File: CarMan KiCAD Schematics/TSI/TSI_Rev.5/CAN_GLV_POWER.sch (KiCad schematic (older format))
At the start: 50 parts, among them J31 Cooling Jumper, K2 G5LE-1-E, K3 SFS2-DC24V, K4 SFS2-DC24V, Q11 TN2130K1-G, U14 Bottom Left, U15 Top Left, U17 Top Right, U2 Bottom Right, U20 TLP293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

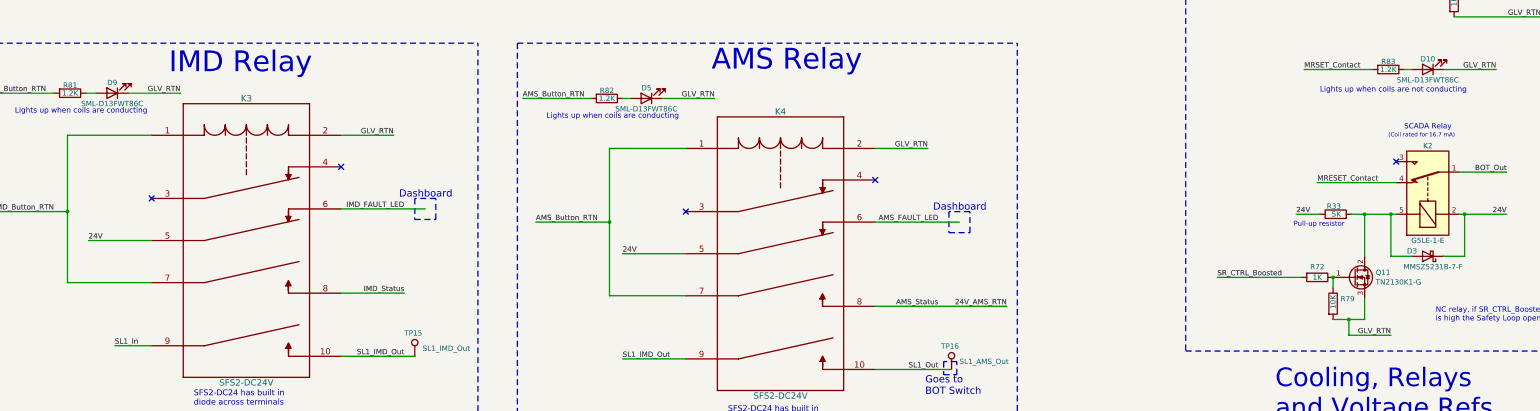
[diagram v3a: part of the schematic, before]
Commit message: - Removed pull up resistor  - Changed the relay leds such that they are the ones logic and GLV Bob use
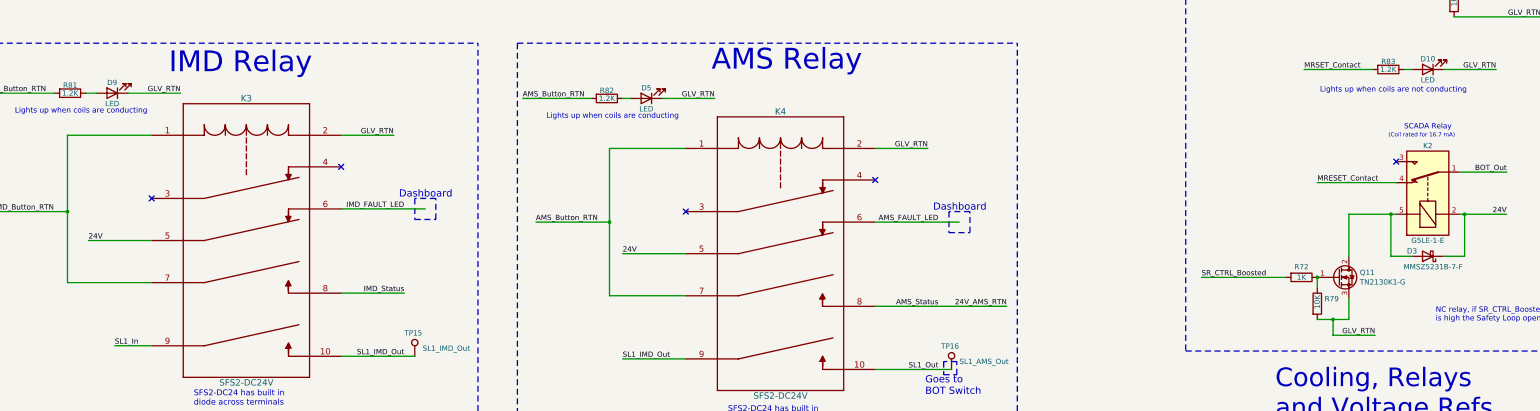
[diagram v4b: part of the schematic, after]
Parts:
- removed R33: 5K, Resistor_SMD:R_0805_2012Metric_Pad1.15x1.40mm_HandSolder, symbol Device:R
- D10, D5, D9: value SML-D13FWT86C -> LED; footprint LED_SMD:LED_0603_1608Metric -> LED_SMD:LED_0805_2012Metric_Pad1.15x1.40mm_HandSolder; Part Name (none) -> VAOL-S8GT4
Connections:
- wire segments 200 -> 198
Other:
- note removed: "Pull-up resistor"
- moved on the sheet: Q11, R72, R79
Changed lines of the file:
@@
 L Device:Q_NMOS_GDS Q11
 U 1 1 5FB4C495
-P 13650 9150
-F 0 "Q11" H 13854 9196 50  0000 L CNN
-F 1 "TN2130K1-G" H 13854 9105 50  0000 L CNN
-F 2 "TSI_Rev_2021_Footprint_Lib:SOT95P237X112-3N" H 13850 9250 50  0001 C CNN
-F 3 "https://ww1.microchip.com/downloads/en/DeviceDoc/TN2130-N-Channel-Enhancement-Mode-Vertical-DMOS-FET-Data-Sheet-20005944B.pdf" H 13650 9150 50  0001 C CNN
-	1    13650 9150
-	1    0    0    -1
-$EndComp
-Text Label 12350 9150 0    50   ~ 0
+P 13500 9150
+F 0 "Q11" H 13704 9196 50  0000 L CNN
+F 1 "TN2130K1-G" H 13704 9105 50  0000 L CNN
+F 2 "TSI_Rev_2021_Footprint_Lib:SOT95P237X112-3N" H 13700 9250 50  0001 C CNN
+F 3 "https://ww1.microchip.com/downloads/en/DeviceDoc/TN2130-N-Channel-Enhancement-Mode-Vertical-DMOS-FET-Data-Sheet-20005944B.pdf" H 13500 9150 50  0001 C CNN
+	1    13500 9150
+	1    0    0    -1
+$EndComp
+Text Label 12200 9150 0    50   ~ 0
 SR_CTRL_Boosted
 $Comp
@@
 L Device:R R72
 U 1 1 5FB6696B
-P 13300 9150
-F 0 "R72" V 13200 9150 50  0000 C CNN
-F 1 "1K" V 13300 9150 50  0000 C CNN
-F 2 "Resistor_SMD:R_0805_2012Metric_Pad1.15x1.40mm_HandSolder" V 13230 9150 50  0001 C CNN
-F 3 "~" H 13300 9150 50  0001 C CNN
-	1    13300 9150
+P 13150 9150
+F 0 "R72" V 13050 9150 50  0000 C CNN
+F 1 "1K" V 13150 9150 50  0000 C CNN
+F 2 "Resistor_SMD:R_0805_2012Metric_Pad1.15x1.40mm_HandSolder" V 13080 9150 50  0001 C CNN
+F 3 "~" H 13150 9150 50  0001 C CNN
+	1    13150 9150
 	0    1    1    0
 $EndComp
 Wire Wire Line
-	13450 9150 13450 9250
-Text Label 14000 9700 2    50   ~ 0
-GLV_RTN
-Connection ~ 13450 9150
-Wire Wire Line
-	13750 9350 13750 9550
-Wire Wire Line
-	13750 9550 13600 9550
-Wire Wire Line
-	13750 8950 13750 8550
-Wire Wire Line
-	13750 8550 14000 8550
+	13300 9150 13300 9250
+Text Label 13850 9700 2    50   ~ 0
+GLV_RTN
+Connection ~ 13300 9150
+Wire Wire Line
+	13600 9350 13600 9550
+Wire Wire Line
+	13600 9550 13450 9550
+Wire Wire Line
+	13600 8950 13600 8550
 Text Label 15100 8550 2    50   ~ 0
 24V
@@
 Safety_Loop
 Wire Wire Line
-	13600 9550 13600 9700
-Wire Wire Line
-	13600 9700 14000 9700
-Connection ~ 13600 9550
-Wire Wire Line
-	13600 9550 13450 9550
-Wire Wire Line
-	12350 9150 13150 9150
+	13450 9550 13450 9700
+Wire Wire Line
+	13450 9700 13850 9700
+Connection ~ 13450 9550
+Wire Wire Line
+	13450 9550 13300 9550
+Wire Wire Line
+	12200 9150 13000 9150
 Text Label 4625 9300 2    50   ~ 0
 IMD_Status
@@
 P 1850 7400
 F 0 "D9" H 1850 7300 50  0000 C CNN
-F 1 "SML-D13FWT86C" H 1850 7500 50  0000 C CNN
-F 2 "LED_SMD:LED_0603_1608Metric" H 1850 7400 50  0001 C CNN
-F 3 "~" H 1850 7400 50  0001 C CNN
+F 1 "LED" H 1850 7500 50  0000 C CNN
+F 2 "LED_SMD:LED_0805_2012Metric_Pad1.15x1.40mm_HandSolder" H 1850 7400 50  0001 C CNN
+F 3 "http://static.vcclite.com/pdf/VAOL-S8GT4-LED-0805-green.pdf" H 1850 7400 50  0001 C CNN
+F 4 "VAOL-S8GT4" H 1850 7400 50  0001 C CNN "Part Name"
 	1    1850 7400
 	-1   0    0    1
@@
 P 6925 7450
 F 0 "D5" H 6925 7350 50  0000 C CNN
-F 1 "SML-D13FWT86C" H 6925 7550 50  0000 C CNN
-F 2 "LED_SMD:LED_0603_1608Metric" H 6925 7450 50  0001 C CNN
-F 3 "~" H 6925 7450 50  0001 C CNN
+F 1 "LED" H 6925 7550 50  0000 C CNN
+F 2 "LED_SMD:LED_0805_2012Metric_Pad1.15x1.40mm_HandSolder" H 6925 7450 50  0001 C CNN
+F 3 "http://static.vcclite.com/pdf/VAOL-S8GT4-LED-0805-green.pdf" H 6925 7450 50  0001 C CNN
+F 4 "VAOL-S8GT4" H 6925 7450 50  0001 C CNN "Part Name"
 	1    6925 7450
 	-1   0    0    1
@@
 P 14350 7175
 F 0 "D10" H 14350 7075 50  0000 C CNN
-F 1 "SML-D13FWT86C" H 14350 7275 50  0000 C CNN
-F 2 "LED_SMD:LED_0603_1608Metric" H 14350 7175 50  0001 C CNN
-F 3 "~" H 14350 7175 50  0001 C CNN
+F 1 "LED" H 14350 7275 50  0000 C CNN
+F 2 "LED_SMD:LED_0805_2012Metric_Pad1.15x1.40mm_HandSolder" H 14350 7175 50  0001 C CNN
+F 3 "http://static.vcclite.com/pdf/VAOL-S8GT4-LED-0805-green.pdf" H 14350 7175 50  0001 C CNN
+F 4 "VAOL-S8GT4" H 14350 7175 50  0001 C CNN "Part Name"
 	1    14350 7175
 	-1   0    0    1
@@
 L Device:R R79
 U 1 1 5FB66337
-P 13450 9400
-F 0 "R79" H 13520 9446 50  0000 L CNN
-F 1 "10K" V 13450 9350 50  0000 L CNN
-F 2 "Resistor_SMD:R_0805_2012Metric_Pad1.15x1.40mm_HandSolder" V 13380 9400 50  0001 C CNN
-F 3 "~" H 13450 9400 50  0001 C CNN
-	1    13450 9400
-	1    0    0    -1
-$EndComp
-$Comp
-L Device:R R33
-U 1 1 6090AD09
-P 13475 8550
-F 0 "R33" V 13550 8500 50  0000 L CNN
-F 1 "5K" V 13475 8500 50  0000 L CNN
-F 2 "Resistor_SMD:R_0805_2012Metric_Pad1.15x1.40mm_HandSolder" V 13405 8550 50  0001 C CNN
-F 3 "~" H 13475 8550 50  0001 C CNN
-	1    13475 8550
-	0    -1   -1   0
-$EndComp
-Wire Wire Line
-	13750 8550 13625 8550
-Connection ~ 13750 8550
-Wire Wire Line
-	13100 8550 13325 8550
-Text Label 13100 8550 0    50   ~ 0
-24V
-Text Notes 13075 8675 0    47   ~ 0
-Pull-up resistor
+P 13300 9400
+F 0 "R79" H 13370 9446 50  0000 L CNN
+F 1 "10K" V 13300 9350 50  0000 L CNN
+F 2 "Resistor_SMD:R_0805_2012Metric_Pad1.15x1.40mm_HandSolder" V 13230 9400 50  0001 C CNN
+F 3 "~" H 13300 9400 50  0001 C CNN
+	1    13300 9400
+	1    0    0    -1
+$EndComp
 Text Notes 13975 7825 0    39   ~ 0
 (Coil rated for 16.7 mA)
@@
 Text Notes 12400 2200 0    39   ~ 0
 Needs to be\nrated for 1/2W\n
+Wire Wire Line
+	13600 8550 14000 8550
 $EndSCHEMATC

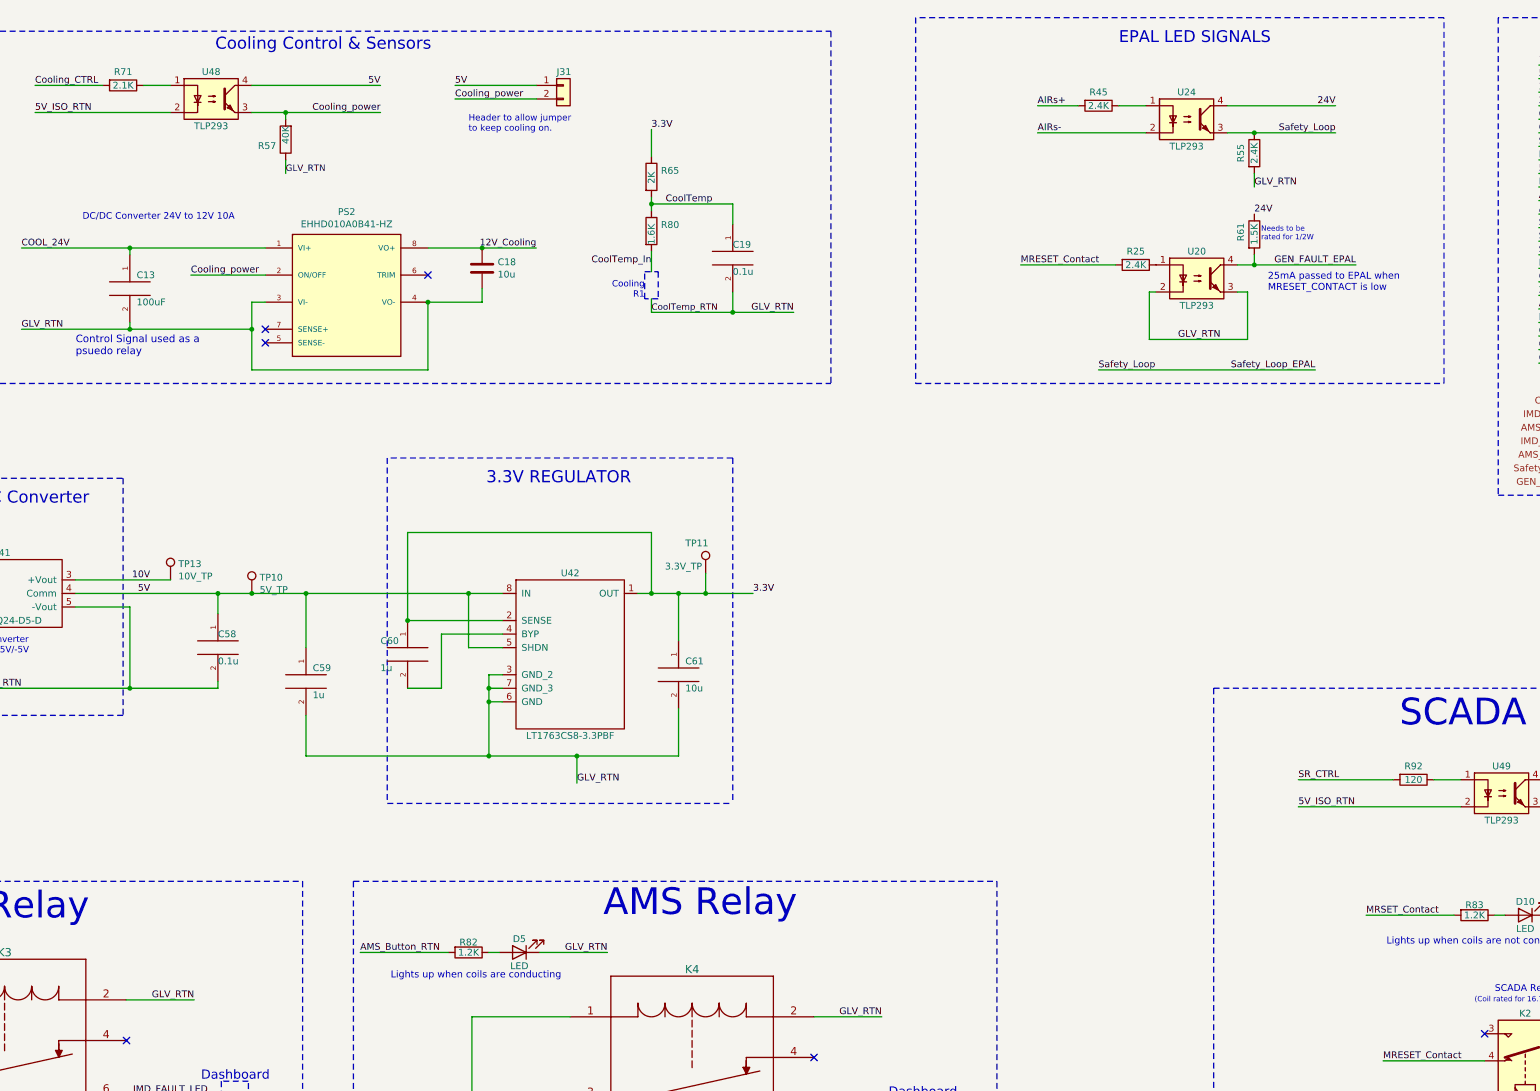
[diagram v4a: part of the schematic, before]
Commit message: Added additional TLP for 24V safety loop for epal moved D14 moved to output of U35
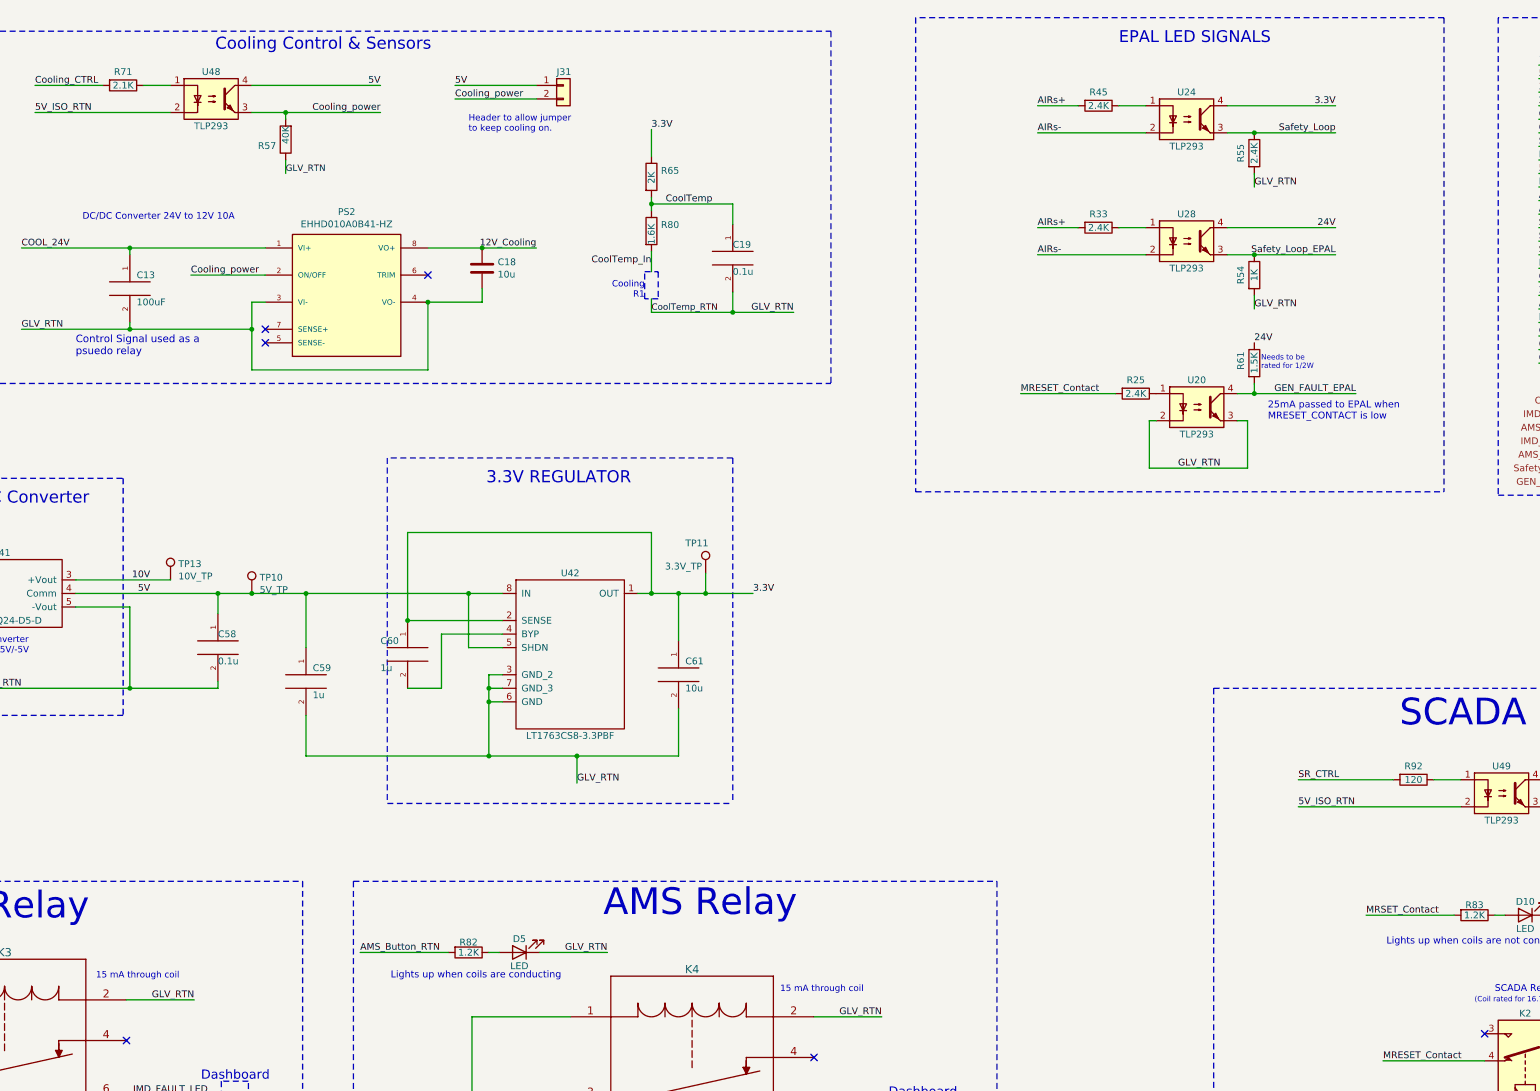
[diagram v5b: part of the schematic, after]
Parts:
- added R33: 2.4K, Resistor_SMD:R_0805_2012Metric_Pad1.15x1.40mm_HandSolder, symbol Device:R
- added R54: 1K, Resistor_SMD:R_0805_2012Metric_Pad1.15x1.40mm_HandSolder, symbol Device:R
- added U28: TLP293, Package_SO:SOIC-4_4.55x2.6mm_P1.27mm, symbol TSI_Rev.5-rescue:TLP293-CarMan_KiCAD_Library-TSI_Rev.5-rescue
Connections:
- wire segments 198 -> 204
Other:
- note added: "15 mA through coil"
- moved on the sheet: R25, R61, U20
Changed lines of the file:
@@
 Wire Wire Line
 	4950 1050 5900 1050
-Text Label 11200 3150 0    50   ~ 0
-Safety_Loop
 Wire Wire Line
 	13450 9550 13450 9700
@@
 Wire Notes Line
 	2950 650  2950 3250
-Text Label 10625 2375 0    50   ~ 0
+Text Label 10625 3325 0    50   ~ 0
 MRESET_Contact
 Text HLabel 14950 3875 0    50   Input ~ 0
@@
 Wire Wire Line
 	12350 1700 12350 1800
-Text Label 12800 3150 2    50   ~ 0
+Text Label 12950 2300 2    50   ~ 0
 Safety_Loop_EPAL
 $Comp
 L TSI_Rev.5-rescue:TLP293-CarMan_KiCAD_Library-TSI_Rev.5-rescue U20
 U 1 1 6012F5F3
-P 11925 2475
-F 0 "U20" H 11925 2675 50  0000 C CNN
-F 1 "TLP293" H 11925 2275 50  0000 C CNN
-F 2 "Package_SO:SOIC-4_4.55x2.6mm_P1.27mm" H 11725 2275 50  0001 L CIN
-F 3 "https://www.mouser.com/ProductDetail/Toshiba/TLP293GB-TPLE/?qs=OLJpxlzHOSSc5RAOktTSWw%3D%3D" H 11925 2475 50  0001 L CNN
-	1    11925 2475
+P 11925 3425
+F 0 "U20" H 11925 3625 50  0000 C CNN
+F 1 "TLP293" H 11925 3225 50  0000 C CNN
+F 2 "Package_SO:SOIC-4_4.55x2.6mm_P1.27mm" H 11725 3225 50  0001 L CIN
+F 3 "https://www.mouser.com/ProductDetail/Toshiba/TLP293GB-TPLE/?qs=OLJpxlzHOSSc5RAOktTSWw%3D%3D" H 11925 3425 50  0001 L CNN
+	1    11925 3425
 	1    0    0    -1
 $EndComp
@@
 L Device:R R25
 U 1 1 60131E61
-P 11475 2375
-F 0 "R25" V 11375 2375 50  0000 C CNN
-F 1 "2.4K" V 11475 2375 50  0000 C CNN
-F 2 "Resistor_SMD:R_0805_2012Metric_Pad1.15x1.40mm_HandSolder" V 11405 2375 50  0001 C CNN
-F 3 "~" H 11475 2375 50  0001 C CNN
-	1    11475 2375
+P 11475 3325
+F 0 "R25" V 11375 3325 50  0000 C CNN
+F 1 "2.4K" V 11475 3325 50  0000 C CNN
+F 2 "Resistor_SMD:R_0805_2012Metric_Pad1.15x1.40mm_HandSolder" V 11405 3325 50  0001 C CNN
+F 3 "~" H 11475 3325 50  0001 C CNN
+	1    11475 3325
 	0    1    1    0
 $EndComp
 Wire Wire Line
-	12225 2575 12300 2575
-Text Label 12100 2925 2    50   ~ 0
-GLV_RTN
-Wire Wire Line
-	11625 2575 11575 2575
-Wire Wire Line
-	11575 2575 11575 2925
+	12225 3525 12300 3525
+Text Label 12100 3875 2    50   ~ 0
+GLV_RTN
+Wire Wire Line
+	11625 3525 11575 3525
+Wire Wire Line
+	11575 3525 11575 3875
 $Comp
 L Connector_Generic:Conn_01x02 J?
@@
 	12050 5500 15950 5500
 Wire Notes Line
-	9850 3250 13750 3250
-Wire Notes Line
-	13750 3250 13750 550
-Wire Notes Line
 	13750 550  9850 550
-Wire Notes Line
-	9850 550  9850 3250
 Text Notes 11350 750  0    87   ~ 0
 EPAL LED SIGNALS
@@
 Wire Wire Line
 	11550 1200 11350 1200
-Text Label 12950 1200 2    50   ~ 0
+Text Label 12950 2100 2    50   ~ 0
 24V
 Wire Wire Line
 	12950 1200 12150 1200
-Wire Wire Line
-	11200 3150 12800 3150
 Wire Wire Line
 	6700 9925 7300 9925
@@
 L Device:R R61
 U 1 1 601328F4
-P 12350 2150
-F 0 "R61" V 12250 2100 50  0000 L CNN
-F 1 "1.5K" V 12350 2075 50  0000 L CNN
-F 2 "Resistor_SMD:R_0805_2012Metric_Pad1.15x1.40mm_HandSolder" V 12280 2150 50  0001 C CNN
-F 3 "~" H 12350 2150 50  0001 C CNN
-	1    12350 2150
-	1    0    0    -1
-$EndComp
-Text Label 12350 2000 0    50   ~ 0
+P 12350 3100
+F 0 "R61" V 12250 3050 50  0000 L CNN
+F 1 "1.5K" V 12350 3025 50  0000 L CNN
+F 2 "Resistor_SMD:R_0805_2012Metric_Pad1.15x1.40mm_HandSolder" V 12280 3100 50  0001 C CNN
+F 3 "~" H 12350 3100 50  0001 C CNN
+	1    12350 3100
+	1    0    0    -1
+$EndComp
+Text Label 12350 2950 0    50   ~ 0
 24V
-Text Label 13100 2375 2    50   ~ 0
+Text Label 13100 3325 2    50   ~ 0
 GEN_FAULT_EPAL
 Wire Wire Line
-	12225 2375 12350 2375
-Wire Wire Line
-	12350 2375 12350 2300
-Connection ~ 12350 2375
-Wire Wire Line
-	12350 2375 13100 2375
-Wire Wire Line
-	12300 2575 12300 2925
-Wire Wire Line
-	11575 2925 12300 2925
-Text Notes 12450 2575 0    51   ~ 0
+	12225 3325 12350 3325
+Wire Wire Line
+	12350 3325 12350 3250
+Connection ~ 12350 3325
+Wire Wire Line
+	12350 3325 13100 3325
+Wire Wire Line
+	12300 3525 12300 3875
+Wire Wire Line
+	11575 3875 12300 3875
+Text Notes 12450 3525 0    51   ~ 0
 25mA passed to EPAL when\nMRESET_CONTACT is low
 Wire Notes Line
@@
 	9750 9950 9750 10075
 Wire Wire Line
-	10625 2375 11325 2375
+	10625 3325 11325 3325
 $Comp
 L Device:R R79
@@
 Wire Wire Line
 	14700 8550 15100 8550
-Text Notes 12400 2200 0    39   ~ 0
+Text Notes 12400 3150 0    39   ~ 0
 Needs to be\nrated for 1/2W\n
 Wire Wire Line
 	13600 8550 14000 8550
+Text Label 10750 2300 0    50   ~ 0
+AIRs-
+Text Label 10750 2100 0    50   ~ 0
+AIRs+
+Wire Wire Line
+	11550 2300 10750 2300
+Wire Wire Line
+	11050 2100 10750 2100
+$Comp
+L Device:R R33
+U 1 1 60637A88
+P 11200 2100
+F 0 "R33" V 11100 2100 50  0000 C CNN
+F 1 "2.4K" V 11200 2100 50  0000 C CNN
+F 2 "Resistor_SMD:R_0805_2012Metric_Pad1.15x1.40mm_HandSolder" V 11130 2100 50  0001 C CNN
+F 3 "~" H 11200 2100 50  0001 C CNN
+	1    11200 2100
+	0    1    1    0
+$EndComp
+$Comp
+L Device:R R54
+U 1 1 60637A8E
+P 12350 2450
+F 0 "R54" V 12250 2450 50  0000 C CNN
+F 1 "1K" V 12350 2450 50  0000 C CNN
+F 2 "Resistor_SMD:R_0805_2012Metric_Pad1.15x1.40mm_HandSolder" V 12280 2450 50  0001 C CNN
+F 3 "~" H 12350 2450 50  0001 C CNN
+	1    12350 2450
+	1    0    0    -1
+$EndComp
+$Comp
+L TSI_Rev.5-rescue:TLP293-CarMan_KiCAD_Library-TSI_Rev.5-rescue U28
+U 1 1 60637A94
+P 11850 2200
+F 0 "U28" H 11850 2400 50  0000 C CNN
+F 1 "TLP293" H 11850 2000 50  0000 C CNN
+F 2 "Package_SO:SOIC-4_4.55x2.6mm_P1.27mm" H 11650 2000 50  0001 L CIN
+F 3 "" H 11850 2200 50  0001 L CNN
+	1    11850 2200
+	1    0    0    -1
+$EndComp
+Text Label 12350 2700 0    50   ~ 0
+GLV_RTN
+Wire Wire Line
+	12350 2600 12350 2700
+Connection ~ 12350 2300
+Wire Wire Line
+	12150 2300 12350 2300
+Wire Wire Line
+	12350 2300 12950 2300
+Wire Wire Line
+	11550 2100 11350 2100
+Text Label 12950 1200 2    50   ~ 0
+3.3V
+Wire Wire Line
+	12950 2100 12150 2100
+Wire Notes Line
+	13750 550  13750 4050
+Wire Notes Line
+	9850 4050 13750 4050
+Wire Notes Line
+	9850 550  9850 4050
+Text Notes 3800 7650 0    47   ~ 0
+15 mA through coil
+Text Notes 8850 7750 0    47   ~ 0
+15 mA through coil
 $EndSCHEMATC
